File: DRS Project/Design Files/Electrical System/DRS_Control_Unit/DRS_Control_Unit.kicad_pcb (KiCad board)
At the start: 2 copper layers, 100 x 100 mm, 37 parts, among them IC1 AP63301QWU-7, J1 Deutsch DT, J2 Screw, J3 Servo, J5 DE9_Socket, SW1 DSIC01THGET, U1 AMS1117, U7 Teensy4.0-NU-Teams, U8 TJA1051T-3

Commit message: improved PCB design (still unfinished)
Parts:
- removed J5: DE9_Socket, Connector_Dsub:DSUB-9_Socket_Vertical_P2.77x2.84mm
- added J4: DE9_Socket_MountingHoles, Connector_Dsub:DSUB-9_Socket_Vertical_P2.77x2.84mm_MountingHoles, F.Cu at (207.4, 42.2)
- added R5: 9k, Resistor_SMD:R_1206_3216Metric_Pad1.30x1.75mm_HandSolder, F.Cu at (161.2, 59.5)
- C3: value C4 -> 47p
- C7: value 0.1uF -> 100n
- L1: value 4.7u -> 10u
- R6: renamed from R5; value 9k -> SOCKET
- R7: renamed from R6; footprint Resistor_SMD:R_1206_3216Metric_Pad1.30x1.75mm_HandSolder -> Resistor_SMD:R_1206_3216Metric
- R8: renamed from R7; value 120Ω -> 120; footprint Resistor_SMD:R_1206_3216Metric -> Resistor_SMD:R_1206_3216Metric_Pad1.30x1.75mm_HandSolder
- moved C1 149.0 mm to (178.7, 42.0)
- moved D4 149.0 mm to (178.7, 47.5)
- moved R3 149.0 mm to (174.7, 51.0)
- moved U1 149.0 mm to (172.0, 45.5)
- moved J2 147.3 mm to (184.5, 113.9)
- moved D2 132.8 mm to (155.2, 86.0)
- moved D3 132.8 mm to (160.7, 86.0)
- moved F1 132.8 mm to (158.4, 80.5)
- moved J1 132.8 mm to (146.5, 81.0)
- moved R1 132.8 mm to (155.7, 90.0)
- moved R2 132.8 mm to (160.6, 90.0)
- moved C2 120.8 mm to (163.0, 63.5)
- moved C3 120.8 mm to (156.0, 66.6)
- moved C4 120.8 mm to (168.0, 68.0)
- moved C5 120.8 mm to (163.0, 70.5)
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- renumbered C5 to C4, C4 to C5, J2 to J1, J1 to J2, U7 to U2, U8 to U3
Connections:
- net +6V renamed +(VAR)V

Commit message: pcb rev 1 actually complete (fr this time)
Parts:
- added D8: +(VAR)V U.F., LED_SMD:LED_1206_3216Metric_Pad1.42x1.75mm_HandSolder, F.Cu at (95.2, 51.2)
- added D9: +(VAR)V F, LED_SMD:LED_1206_3216Metric_Pad1.42x1.75mm_HandSolder, F.Cu at (95.2, 54.6)
- added R10: 680R, Resistor_SMD:R_1206_3216Metric_Pad1.30x1.75mm_HandSolder, F.Cu at (95.1, 61.2)
- added R11: 680R, Resistor_SMD:R_1206_3216Metric_Pad1.30x1.75mm_HandSolder, F.Cu at (95.1, 57.9)
- added TP3: +5V Regulated., TestPoint:TestPoint_Loop_D1.80mm_Drill1.0mm_Beaded, F.Cu at (89.8, 61.1)
- added TP4: +12V Fused, TestPoint:TestPoint_Loop_D1.80mm_Drill1.0mm_Beaded, F.Cu at (89.8, 51.8)
- added TP5: Ground, TestPoint:TestPoint_Loop_D1.80mm_Drill1.0mm_Beaded, F.Cu at (89.8, 56.5)
- added TP6: Servo Signal, TestPoint:TestPoint_Loop_D1.80mm_Drill1.0mm_Beaded, F.Cu at (89.8, 70.4)
- added TP7: +(VAR)V Regulated, TestPoint:TestPoint_Loop_D1.80mm_Drill1.0mm_Beaded, F.Cu at (89.8, 65.8)
- J4: value DE9_Socket_MountingHoles -> DE-9 Socket
- renumbered C7 to C10, C1 to C4, C2 to C5, C3 to C6, C4 to C7, C5 to C8, C6 to C9, D1 to D3, D2 to D4, D3 to D5, D4 to D6, D5 to D7, F1 to F2, F2 to F3, J3 to J2, J2 to J3, L1 to L2, R7 to R12, R8 to R13, R1 to R4, R2 to R5, R3 to R6, R4 to R7, R5 to R8, R6 to R9, TP1 to TP8, TP2 to TP9, U1 to U2, U2 to U3, U3 to U4

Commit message: improved pcb design (unfinished)
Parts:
- moved TP5 117.9 mm to (207.8, 57.5)
- moved TP7 92.1 mm to (181.8, 71.2), turned to 180 degrees
- moved D9 84.5 mm to (177.8, 72.7), turned to -90 degrees
- moved R11 83.1 mm to (177.8, 67.2), turned to 90 degrees
- moved TP6 75.3 mm to (163.2, 87.2)
- moved D8 70.5 mm to (163.7, 67.7), turned to 90 degrees
- moved R10 69.6 mm to (163.7, 73.2), turned to 90 degrees
- moved J4 67.0 mm to (209.2, 109.1), turned to 90 degrees
- moved TP4 66.3 mm to (146.8, 85.6), turned to 90 degrees
- moved D3 65.1 mm to (161.0, 57.5), turned to -90 degrees
- moved TP3 53.1 mm to (142.5, 54.8)
- moved TP8 27.7 mm to (221.5, 106.5)
- moved J2 26.5 mm to (169.1, 81.5)
- moved C4 25.4 mm to (156.2, 53.7)
- moved D6 25.4 mm to (156.2, 59.2)
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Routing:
- net /CAN HIGH: track 0.00 -> 134.9 mm
- net /CAN LOW: track 0.00 -> 85.8 mm
- net +5V: track 0.00 -> 64.1 mm
- net /VIN: track 0.00 -> 59.2 mm
- net +12V: track 0.00 -> 57.3 mm
- net Net-(D8-A): track 0.00 -> 54.8 mm
- net /SIGNAL: track 0.00 -> 46.0 mm
- net +(VAR)V: track 0.00 -> 25.4 mm
- net Net-(IC1-FB): track 0.00 -> 20.4 mm
- net Net-(D7-K): track 0.00 -> 18.4 mm
- net Net-(D3-A): track 0.00 -> 17.4 mm
- net /RX: track 0.00 -> 15.1 mm
- net /TX: track 0.00 -> 15.1 mm
- net Net-(IC1-SW): track 0.00 -> 8.23 mm
- net Net-(R13-Pad2): track 0.00 -> 4.33 mm
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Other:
- board text added: "HIGH"
- board text added: "LOW"

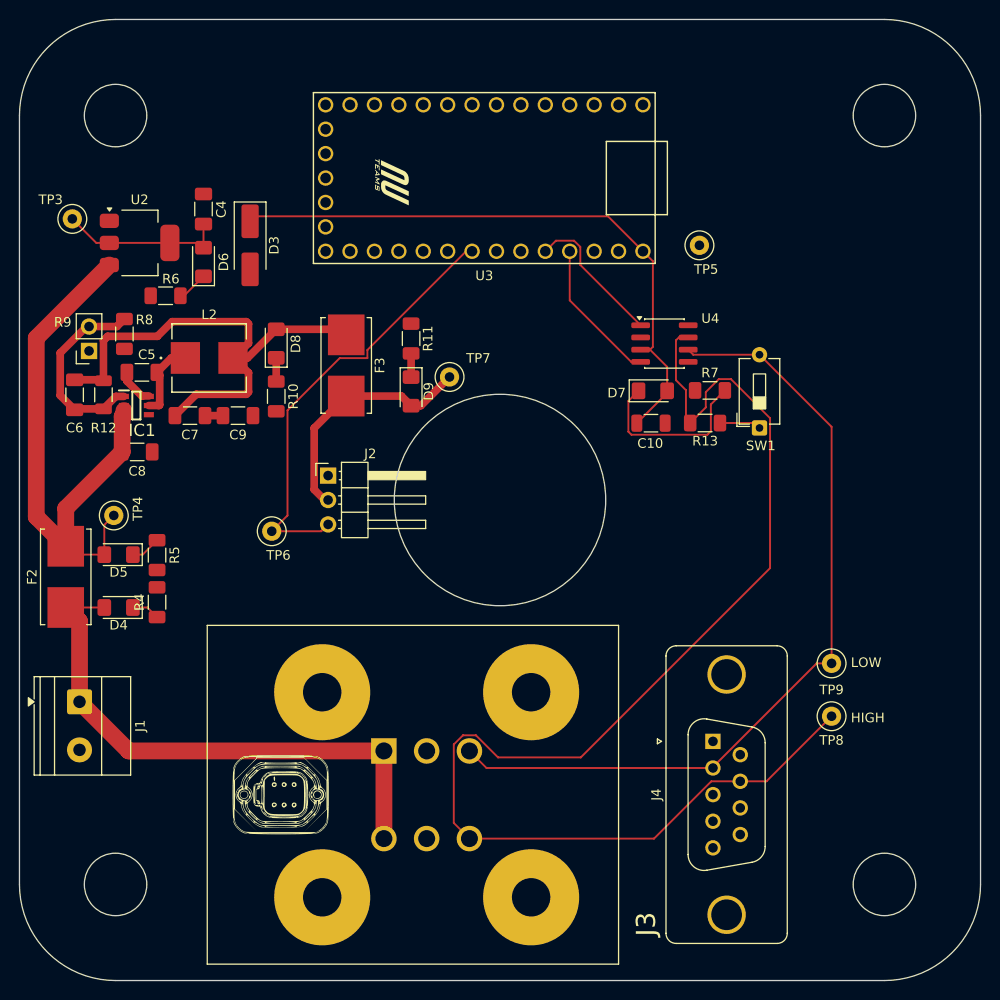
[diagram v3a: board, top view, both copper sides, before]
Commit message: DDR half done for PCB
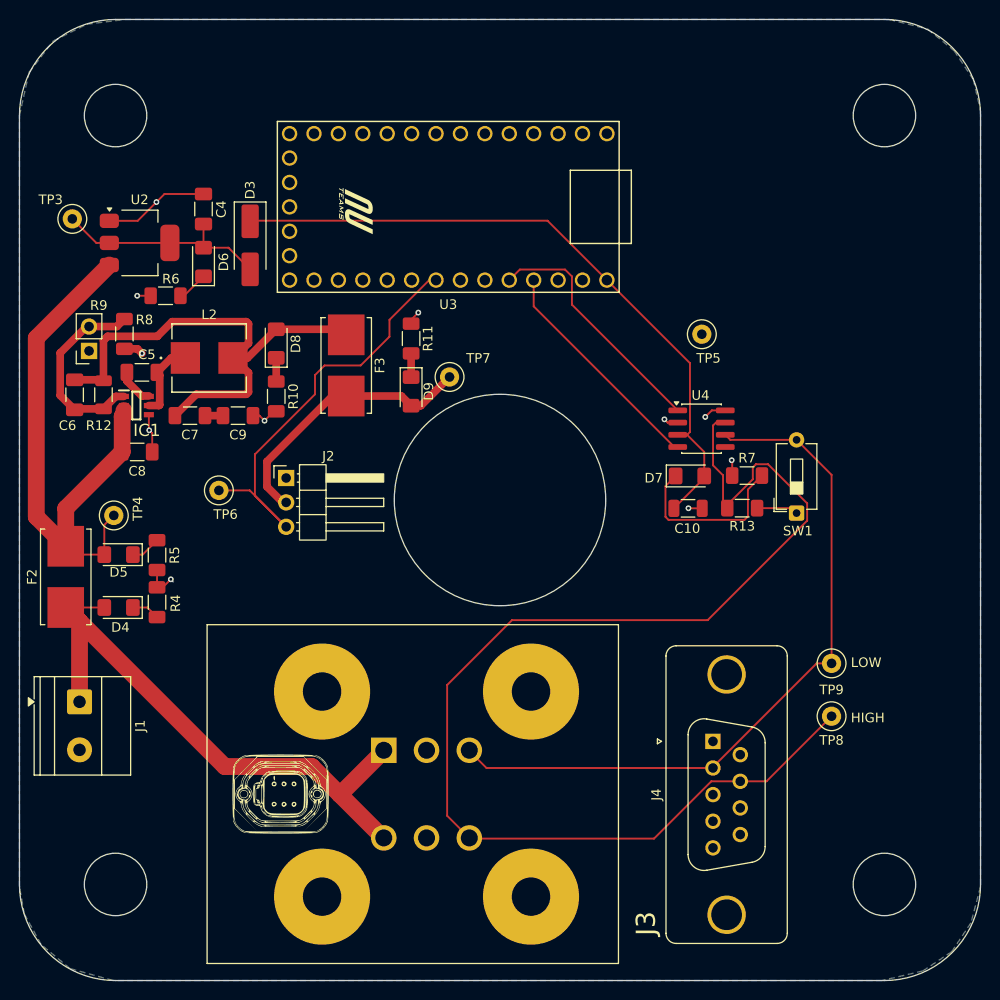
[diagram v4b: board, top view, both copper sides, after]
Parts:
- moved R7 9.66 mm to (212.7, 81.5)
- moved SW1 9.66 mm to (217.9, 85.4)
- moved U4 9.66 mm to (208.0, 76.6)
- moved C10 9.66 mm to (206.6, 84.9)
- moved D7 9.66 mm to (206.8, 81.5)
- moved R13 9.66 mm to (212.2, 84.8)
- moved TP5 9.25 mm to (208.0, 66.8)
- moved TP6 6.95 mm to (157.8, 83.0)
- moved U3 4.80 mm to (198.1, 45.9)
- moved J2 4.37 mm to (164.8, 81.7)
- moved J3 0.07 mm to (177.3, 114.6)
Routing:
- net GND: track 0.00 -> 33.8 mm, vias 0 -> 11
- net /TX: track 15.1 -> 25.8 mm
- net /CAN LOW: track 85.8 -> 75.4 mm
- net /RX: track 15.1 -> 23.8 mm
- net +12V: track 57.3 -> 63.9 mm
- net +5V: track 64.1 -> 70.2 mm
- net Net-(D3-A): track 17.4 -> 23.1 mm
- net /CAN HIGH: track 134.9 -> 129.6 mm
- net +(VAR)V: track 25.4 -> 28.8 mm
- added copper zone on B.Cu, net GND

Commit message: um
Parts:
- moved TP5 4.74 mm to (212.5, 65.2)
- moved U3 2.66 mm to (199.9, 43.9)
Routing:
- net +5V: track 70.2 -> 72.3 mm
- net /RX: track 23.8 -> 25.4 mm
- net /SIGNAL: track 46.0 -> 45.0 mm
- net /TX: track 25.8 -> 26.5 mm
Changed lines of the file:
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@@
 	(footprint "TestPoint:TestPoint_Loop_D1.80mm_Drill1.0mm_Beaded"
 		(layer "F.Cu")
-		(at 208 66.75)
+		(at 212.5 65.25)
 		(descr "wire loop with bead as test point, loop diameter 1.8mm, hole diameter 1.0mm")
 		(tags "test point wire loop bead")
@@
 	(footprint "NU-Teams-Footprints:Teensy4.0-NU-Teams"
 		(layer "F.Cu")
-		(at 198.125 45.88 -90)
+		(at 199.875 43.88 -90)
 		(property "Reference" "U3"
 			(at 17.78 16.51 0)
@@
 	)
 	(segment
-		(start 168.75 70)
-		(end 172.5 70)
-		(width 0.2)
-		(layer "F.Cu")
-		(net "/SIGNAL")
-	)
-	(segment
-		(start 175.5 67)
-		(end 175.5 65.25)
+		(start 167.75 73)
+		(end 157.75 83)
 		(width 0.2)
 		(layer "F.Cu")
@@
 	)
 	(segment
-		(start 179.63 61.12)
-		(end 180.345 61.12)
+		(start 175.5 65.75)
+		(end 175.5 67)
 		(width 0.2)
 		(layer "F.Cu")
@@
 	)
 	(segment
-		(start 175.5 65.25)
-		(end 179.63 61.12)
+		(start 182.095 59.12)
+		(end 182.095 59.155)
 		(width 0.2)
 		(layer "F.Cu")
@@
 	)
 	(segment
-		(start 161.5 79.25)
-		(end 167.75 73)
+		(start 172.5 70)
+		(end 168.25 70)
 		(width 0.2)
 		(layer "F.Cu")
@@
 	)
 	(segment
-		(start 172.5 70)
-		(end 175.5 67)
+		(start 167.75 70.5)
+		(end 167.75 73)
 		(width 0.2)
 		(layer "F.Cu")
@@
 	)
 	(segment
-		(start 167.75 71)
-		(end 168.75 70)
+		(start 182.095 59.155)
+		(end 175.5 65.75)
 		(width 0.2)
 		(layer "F.Cu")
@@
 	)
 	(segment
-		(start 167.75 73)
-		(end 167.75 71)
+		(start 175.5 67)
+		(end 172.5 70)
 		(width 0.2)
 		(layer "F.Cu")
@@
 	)
 	(segment
-		(start 164.75 86.79)
-		(end 161.5 83.54)
+		(start 168.25 70)
+		(end 167.75 70.5)
 		(width 0.2)
 		(layer "F.Cu")
@@
 	)
 	(segment
-		(start 161.5 83.54)
-		(end 161.5 79.25)
-		(width 0.2)
-		(layer "F.Cu")
-		(net "/SIGNAL")
-	)
-	(segment
 		(start 177.75 71.2125)
 		(end 177.75 68.75)
@@
 	)
 	(segment
-		(start 187.965 61.12)
-		(end 189.065 60.02)
+		(start 191.585 57.25)
+		(end 192.75 57.25)
 		(width 0.2)
 		(layer "F.Cu")
@@
 	)
 	(segment
-		(start 189.065 60.02)
-		(end 193.77 60.02)
+		(start 193.355 57.855)
+		(end 192.75 57.25)
 		(width 0.2)
 		(layer "F.Cu")
@@
 	)
 	(segment
-		(start 193.77 60.02)
-		(end 194.485 60.735)
+		(start 205.4925 74.677499)
+		(end 193.355 62.539999)
 		(width 0.2)
 		(layer "F.Cu")
@@
 	)
 	(segment
-		(start 194.485 63.669999)
-		(end 205.4925 74.677499)
+		(start 193.355 62.539999)
+		(end 193.355 57.855)
 		(width 0.2)
 		(layer "F.Cu")
@@
 	)
 	(segment
-		(start 194.485 60.735)
-		(end 194.485 63.669999)
+		(start 189.715 59.12)
+		(end 191.585 57.25)
 		(width 0.2)
 		(layer "F.Cu")
@@
 	)
 	(segment
-		(start 198.125 61.12)
-		(end 206.7675 69.7625)
+		(start 206.7675 76.917498)
+		(end 206.7675 70.7675)
 		(width 0.2)
 		(layer "F.Cu")
@@
 	)
 	(segment
-		(start 206.467499 77.217499)
-		(end 205.4925 77.217499)
+		(start 208.25 81.709999)
+		(end 205.0925 84.867499)
 		(width 0.2)
 		(layer "F.Cu")
@@
 	)
 	(segment
-		(start 208.25 81.709999)
-		(end 205.0925 84.867499)
+		(start 206.7675 70.7675)
+		(end 199.875 63.875)
 		(width 0.2)
 		(layer "F.Cu")
@@
 	)
 	(segment
-		(start 161.06 54.94)
-		(end 191.945 54.94)
+		(start 205.4925 77.217499)
+		(end 206.467499 77.217499)
 		(width 0.2)
 		(layer "F.Cu")
@@
 	)
 	(segment
-		(start 208.25 79)
-		(end 208.25 81.497499)
+		(start 199.875 63.875)
+		(end 199.875 59.12)
 		(width 0.2)
 		(layer "F.Cu")
@@
 	)
 	(segment
-		(start 191.945 54.94)
-		(end 198.125 61.12)
+		(start 208.25 79)
+		(end 208.25 81.497499)
 		(width 0.2)
 		(layer "F.Cu")
@@
 	)
 	(segment
-		(start 206.7675 69.7625)
+		(start 195.895 55.14)
+		(end 199.875 59.12)
+		(width 0.2)
+		(layer "F.Cu")
+		(net "+5V")
+	)
+	(segment
+		(start 206.467499 77.217499)
 		(end 206.7675 76.917498)
 		(width 0.2)
@@
 	)
 	(segment
-		(start 161 55)
-		(end 161.06 54.94)
+		(start 161.14 55.14)
+		(end 195.895 55.14)
 		(width 0.2)
 		(layer "F.Cu")
@@
 	)
 	(segment
-		(start 206.467499 77.217499)
-		(end 208.25 79)
+		(start 161 55)
+		(end 161.14 55.14)
 		(width 0.2)
 		(layer "F.Cu")
@@
 	)
 	(segment
-		(start 206.7675 76.917498)
-		(end 206.467499 77.217499)
+		(start 206.467499 77.217499)
+		(end 208.25 79)
 		(width 0.2)
 		(layer "F.Cu")
@@
 	)
 	(segment
-		(start 205.146948 78.487499)
-		(end 205.4925 78.487499)
+		(start 204.517501 78.487499)
+		(end 192.255 66.224998)
 		(width 0.2)
 		(layer "F.Cu")
@@
 	)
 	(segment
-		(start 190.505 63.845551)
-		(end 205.146948 78.487499)
+		(start 192.255 66.224998)
+		(end 192.255 59.12)
 		(width 0.2)
 		(layer "F.Cu")
@@
 	)
 	(segment
-		(start 190.505 61.12)
-		(end 190.505 63.845551)
+		(start 205.4925 78.487499)
+		(end 204.517501 78.487499)
 		(width 0.2)
 		(layer "F.Cu")

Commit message: made minor changes to pcb and *nearly* finished
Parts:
- removed D3: SS34, Diode_SMD:D_SMA_Handsoldering
- added D10: +12V PR, LED_SMD:LED_1206_3216Metric_Pad1.42x1.75mm_HandSolder, F.Cu at (148.5, 84.8)
- added U5: Branding_Block_Racing, NU-Teams-Footprints:BRANDING_RACING, F.Cu at (220.0, 60.5)
- D6: value +5V -> SS54; footprint LED_SMD:LED_1206_3216Metric_Pad1.42x1.75mm_HandSolder -> Diode_SMD:D_SMA_Handsoldering
- D7: value +5V PROT -> +5V
- F2: value 5A -> 4A
- R6: value 330R -> 1.2k
- moved D6 30.7 mm to (142.5, 86.8), turned to -90 degrees
- moved R6 24.7 mm to (153.8, 87.5), turned to -90 degrees
- moved TP7 22.1 mm to (162.2, 81.5)
- moved TP5 15.2 mm to (225.2, 73.5)
- moved TP6 9.57 mm to (164.0, 90.2)
- moved J2 6.87 mm to (171.6, 81.7)
- moved D4 5.45 mm to (149.0, 100.4)
- moved D5 5.45 mm to (149.0, 94.9)
- moved F2 5.45 mm to (143.5, 97.2)
- moved R5 5.45 mm to (153.0, 94.9)
- moved TP4 5.45 mm to (148.5, 90.8)
- moved R4 5.45 mm to (153.0, 99.8)
- moved D9 3.43 mm to (176.0, 69.8)
- moved R11 3.43 mm to (176.0, 64.2)
- moved F3 2.55 mm to (170.5, 67.5)
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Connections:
- C4 pad 1: Net-(D3-A) -> +5V
- D5 pad 2: /VIN -> Net-(D5-A)
- D6 pad 1: Net-(D6-K) -> /VIN
- D6 pad 2: Net-(D3-A) -> Net-(D5-A)
- F2 pad 2: /VIN -> Net-(D5-A)
- R6 pad 1: GND -> Net-(D10-K)
- R6 pad 2: Net-(D6-K) -> GND
- TP3 pad 1: Net-(D3-A) -> +5V
- TP4 pad 1: /VIN -> Net-(D5-A)
- U2 pad 2: Net-(D3-A) -> +5V
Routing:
- net Net-(D3-A): track 23.1 -> 0.00 mm
- net +5V: track 72.3 -> 92.6 mm
- net /VIN: track 59.2 -> 45.1 mm
- net Net-(D5-A): track 0.00 -> 14.0 mm
- net +12V: track 63.9 -> 53.8 mm
- net Net-(D10-K): track 0.00 -> 4.24 mm
- net /SIGNAL: track 45.0 -> 41.1 mm
- net Net-(D6-K): track 3.24 -> 0.00 mm
- net GND: track 33.8 -> 36.1 mm
- net Net-(D8-A): track 54.8 -> 53.7 mm
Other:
- board text added: "12V"
- board text added: "GND"

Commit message: updated
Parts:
- added G***: LOGO, LOGO, F.Cu at (68.2, 92.8)
- added G***: LOGO, LOGO, F.Cu at (92.1, 68.4)
- added G***: LOGO, LOGO, F.Cu at (114.3, 68.5)
- added G***: LOGO, LOGO, F.Cu at (45.3, 90.8)
- added G***: LOGO, LOGO, F.Cu at (66.1, 68.9)
- added G***: LOGO, LOGO, F.Cu at (42.3, 66.8)
- C10: footprint Capacitor_SMD:C_1206_3216Metric -> Capacitor_SMD:C_1206_3216Metric_Pad1.33x1.80mm_HandSolder
- J2: footprint Connector_PinHeader_2.54mm:PinHeader_1x03_P2.54mm_Horizontal -> Connector_PinHeader_2.54mm:PinHeader_1x03_P2.54mm_Vertical
- moved R7 59.0 mm to (157.2, 61.6)
- moved C10 57.2 mm to (158.6, 53.7), turned to 90 degrees
- moved D7 54.4 mm to (157.2, 59.1), turned to 180 degrees
- moved TP5 28.7 mm to (201.4, 89.6)
- moved TP4 10.5 mm to (159.0, 90.3)
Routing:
- net Net-(D7-K): track 18.4 -> 2.53 mm
- net Net-(D5-A): track 14.0 -> 22.8 mm
- net /CAN LOW: track 75.4 -> 82.9 mm
- net +5V: track 92.6 -> 86.7 mm
- net +(VAR)V: track 28.8 -> 31.7 mm
- net GND: track 36.1 -> 35.8 mm, vias 11 -> 10
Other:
- board text added: "12V F"
- board text added: "12V PR"
- board text added: "12V UF"
- board text added: "5V"
- board text added: "6-8V"
- board text added: "6-8V F"
- board text added: "6-8V UF"
- board text added: "SIGNAL"

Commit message: Update DRS_Control_Unit.kicad_pcb
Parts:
- added G***: LOGO, LOGO, F.Cu at (93.2, 93.5)
